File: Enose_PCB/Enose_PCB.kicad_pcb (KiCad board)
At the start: 2 copper layers, 128 parts, among them IC1 ISL91127IRNZ-T7A, IC2 MP2722GRH-0000-Z, IC3 TPS22958DGNR, J10 Fan, J5 USB_C_Receptacle_USB2.0_16P, J7 U.FL-R-SMT_01_, J8 U.FL-R-SMT_01_, J9 2229333-2, Q1 Q_NPN, Q2 Q_NPN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

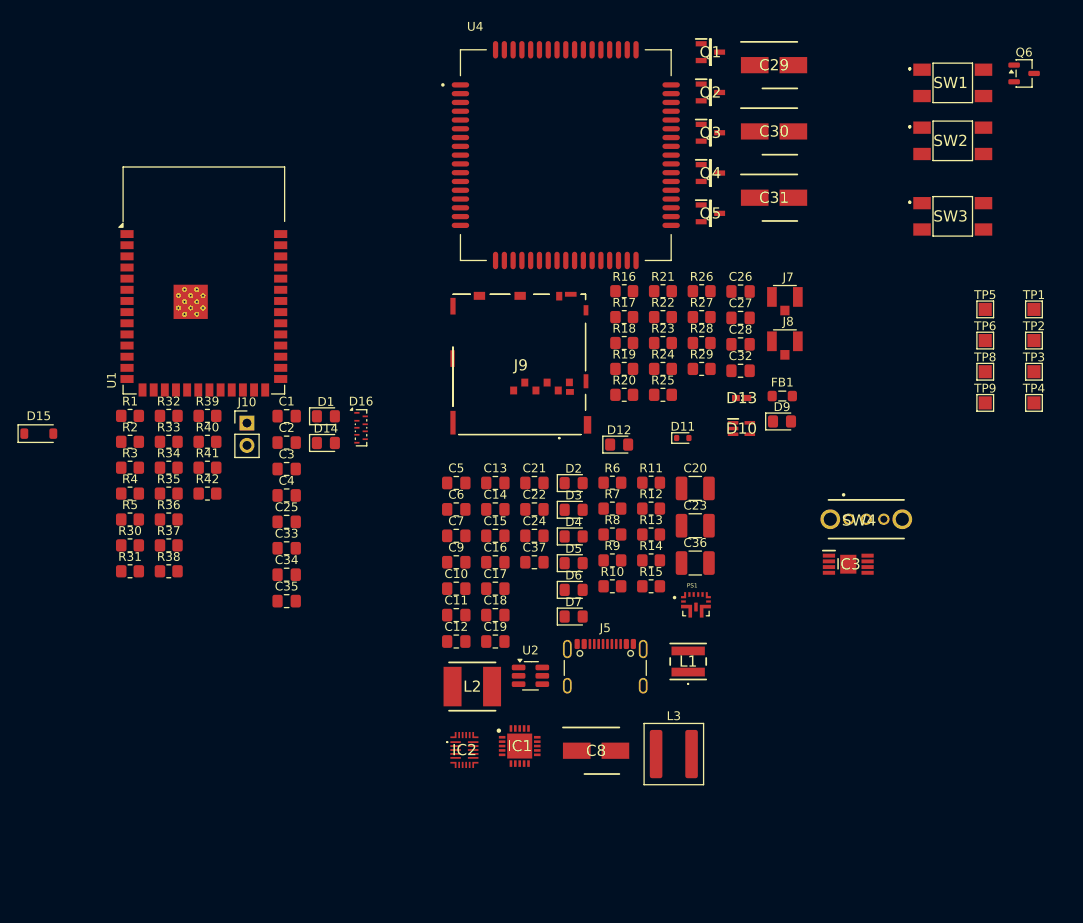
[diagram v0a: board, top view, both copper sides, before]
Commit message: Assigned footprints
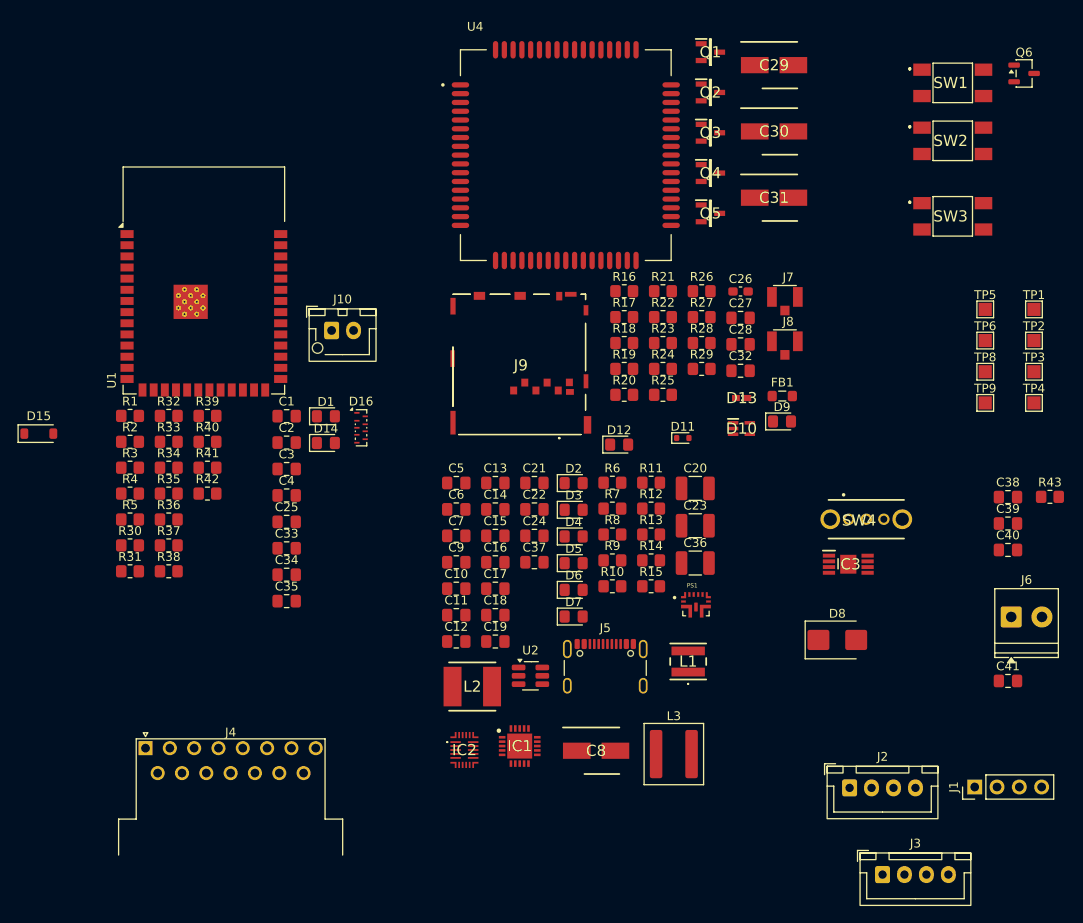
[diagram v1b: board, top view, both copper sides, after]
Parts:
- added C38: 1uF, Capacitor_SMD:C_0805_2012Metric_Pad1.18x1.45mm_HandSolder, F.Cu at (173.3, 89.5)
- added C39: 1500pF, Capacitor_SMD:C_0805_2012Metric_Pad1.18x1.45mm_HandSolder, F.Cu at (173.3, 92.5)
- added C40: 100nF, Capacitor_SMD:C_0805_2012Metric_Pad1.18x1.45mm_HandSolder, F.Cu at (173.3, 95.5)
- added C41: 2.2uF, Capacitor_SMD:C_0805_2012Metric_Pad1.18x1.45mm_HandSolder, F.Cu at (173.3, 110.4)
- added D8: SMBJ18A-E3/52, Diode_SMD:D_SMB, F.Cu at (153.8, 105.8)
- added J1: Conn_01x04_Pin, Connector_PinHeader_2.54mm:PinHeader_1x04_P2.54mm_Vertical, F.Cu at (169.5, 122.5)
- added J2: Conn_01x04_Pin, Connector_JST:JST_XH_B4B-XH-A_1x04_P2.50mm_Vertical, F.Cu at (155.2, 122.6)
- added J3: Conn_01x04_Pin, Connector_JST:JST_XH_B4B-XH-A_1x04_P2.50mm_Vertical, F.Cu at (159.0, 132.5)
- added J4: DA15_Pins, Connector_Dsub:DSUB-15_Pins_Horizontal_P2.77x2.84mm_EdgePinOffset9.40mm, F.Cu at (75.1, 118.1)
- added J6: Battery Terminal, TerminalBlock_Phoenix:TerminalBlock_Phoenix_PT-1,5-2-3.5-H_1x02_P3.50mm_Horizontal, F.Cu at (173.7, 103.1)
- added R43: 100k, Resistor_SMD:R_0805_2012Metric_Pad1.20x1.40mm_HandSolder, F.Cu at (178.1, 89.5)
- C22: value 4.7uF -> 2.2uF
- C25: value 100n -> 100nF
- C26: footprint Capacitor_SMD:C_0805_2012Metric_Pad1.18x1.45mm_HandSolder -> Capacitor_SMD:C_0603_1608Metric_Pad1.08x0.95mm_HandSolder
- J10: footprint Connector_PinHeader_2.54mm:PinHeader_1x02_P2.54mm_Vertical -> Connector_JST:JST_XH_B2B-XH-AM_1x02_P2.50mm_Vertical
- moved J10 14.3 mm to (96.2, 70.5)
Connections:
- C10 pad 2: +BATT -> +SYS
- C37 pad 1: +BATT -> +SYS
- C8 pad 1: +BATT -> +SYS
- C9 pad 1: +BATT -> +SYS
- IC2 pad 13: +BATT -> +SYS
- IC3 pad 1: Net-(IC3-VBIAS) -> +SYS
- IC3 pad 3: Net-(IC3-VBIAS) -> +SYS
- IC3 pad 4: Net-(IC3-VBIAS) -> +SYS
- IC3 pad 5: Net-(IC3-VOUT_1) -> +BATT
- IC3 pad 8: Net-(IC3-VOUT_1) -> +BATT
- L2 pad 1: +BATT -> +SYS
- R7 pad 1: +BATT -> +SYS
- TP2 pad 1: +BATT -> +SYS
